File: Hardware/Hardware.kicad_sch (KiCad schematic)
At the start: 9 parts, among them J1 ILI9341, J2 RJ45_LED_Shielded, SW1 SW_SPST, U1 TMR-0511, U3 Teensy4.1_DEV-16771

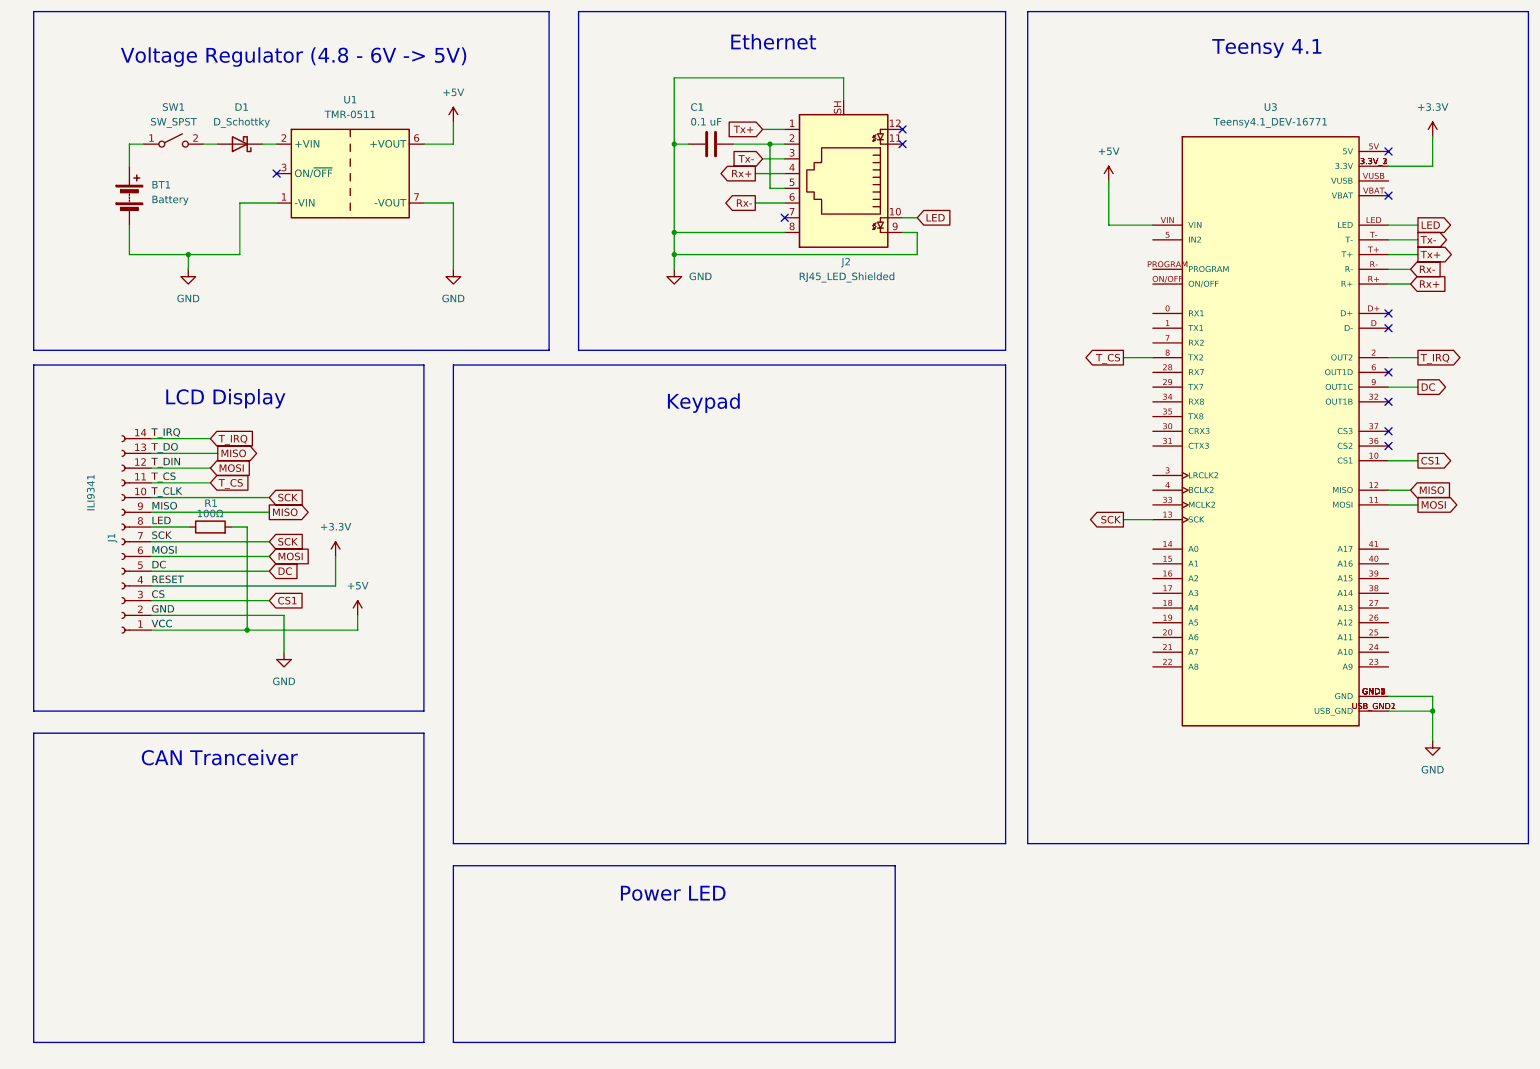
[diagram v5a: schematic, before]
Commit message: Added CAN tranceiver and keypad
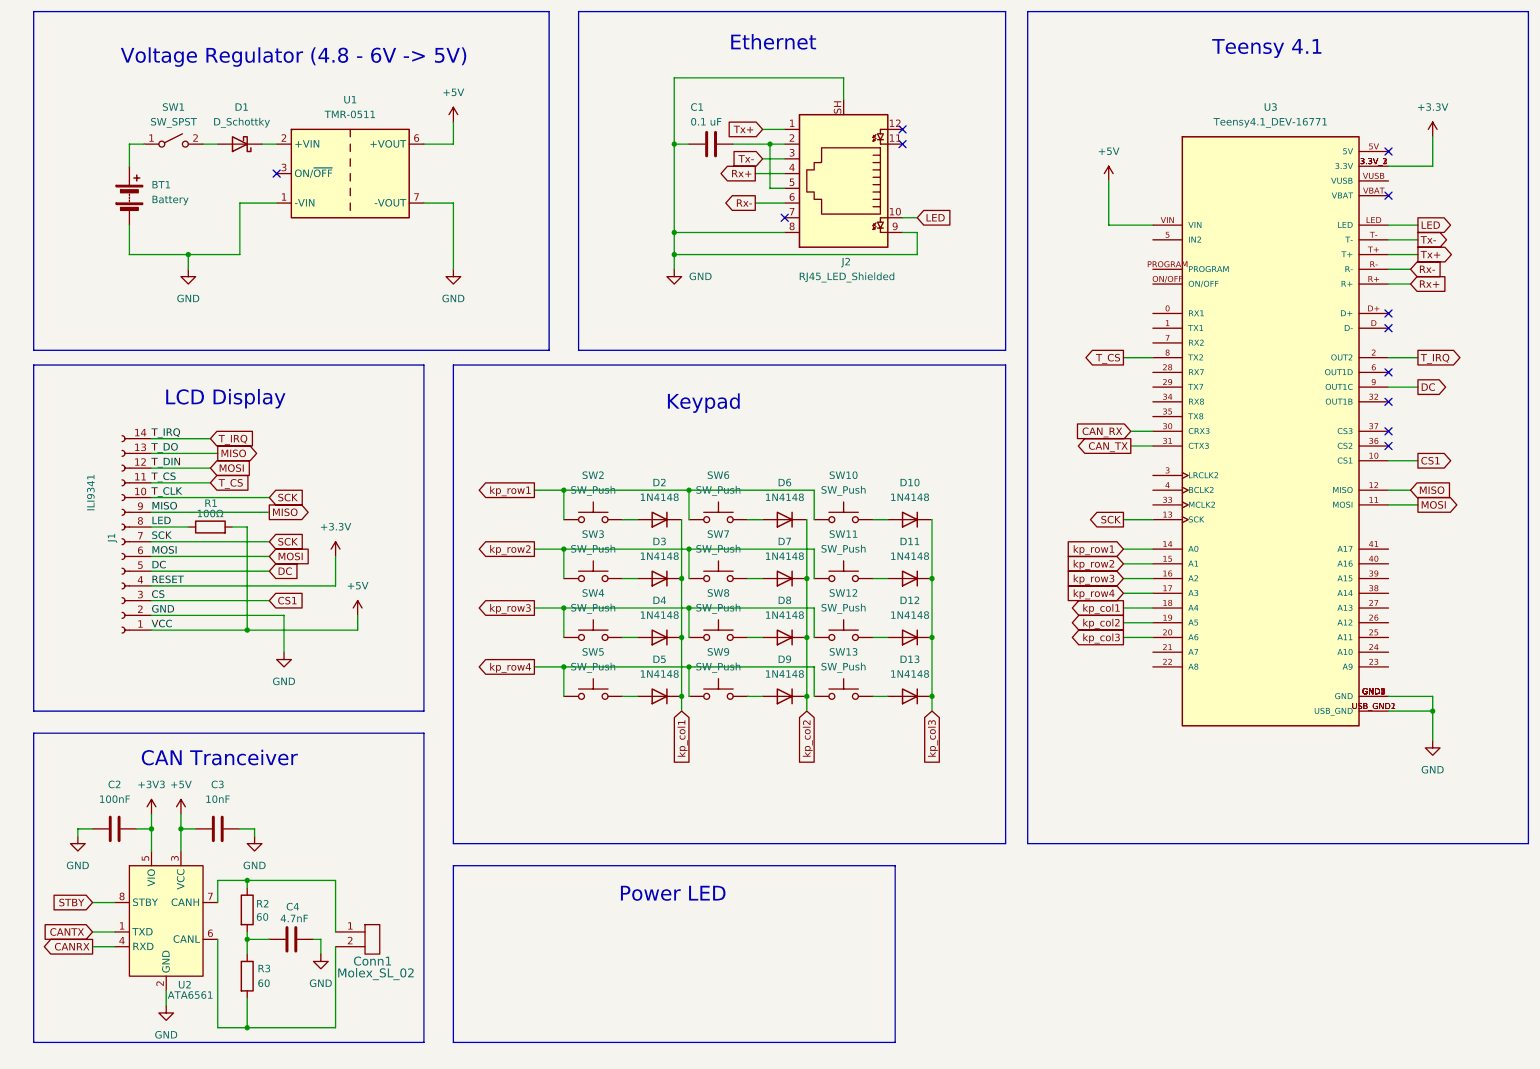
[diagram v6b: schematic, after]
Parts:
- added C2: 100nF, symbol Device:C
- added C3: 10nF, symbol Device:C
- added C4: 4.7nF, symbol Device:C
- added Conn1: Molex_SL_02, symbol MRDT_Connectors:Molex_SL_02
- added D10, D11, D12, D13, D2, D3, D4, D5, D6, D7, D8, D9: 1N4148, Diode_THT:D_DO-35_SOD27_P7.62mm_Horizontal, symbol Diode:1N4148
- added R2, R3: 60, symbol Device:R
- added SW10, SW11, SW12, SW13, SW2, SW3, SW4, SW5, SW6, SW7, SW8, SW9: SW_Push, symbol Switch:SW_Push
- added U2: ATA6561, Package_SO:SOIC-8_3.9x4.9mm_P1.27mm, symbol MRDT_Devices:ATA6561
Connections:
- net +5V: now also C3.1, U2.3 (VCC)
- net GND: now also C2.2, C3.2, C4.2, U2.2 (GND)
- net kp_row1: now reaches U3.14 (A0)
- net kp_row1: now also SW10.1, SW2.1, SW6.1
- net kp_row2: now reaches U3.15 (A1)
- net kp_row2: now also SW11.1, SW3.1, SW7.1
- net kp_row3: now reaches U3.16 (A2)
- net kp_row3: now also SW12.1, SW4.1, SW8.1
- net kp_row4: now reaches U3.17 (A3)
- net kp_row4: now also SW13.1, SW5.1, SW9.1
- net kp_col1: now reaches U3.18 (A4)
- net kp_col1: now also D2.1 (K), D3.1 (K), D4.1 (K), D5.1 (K)
- net kp_col2: now reaches U3.19 (A5)
- net kp_col2: now also D6.1 (K), D7.1 (K), D8.1 (K), D9.1 (K)
- net kp_col3: now reaches U3.20 (A6)
- net kp_col3: now also D10.1 (K), D11.1 (K), D12.1 (K), D13.1 (K)
- net CAN_RX: now reaches U3.30 (CRX3)
- net CAN_TX: now reaches U3.31 (CTX3)
- new net: D5.2 (A), SW5.2
- new net: Conn1.1, R2.1, U2.7 (CANH)
- new net: C4.1, R2.2, R3.1
- new net: D9.2 (A), SW9.2
- new net: D6.2 (A), SW6.2
- new net: D13.2 (A), SW13.2
- new net: D7.2 (A), SW7.2
- new net: D11.2 (A), SW11.2
- new net: D8.2 (A), SW8.2
- new net: Conn1.2, R3.2, U2.6 (CANL)
- new net: D4.2 (A), SW4.2
- new net: D3.2 (A), SW3.2
- new net: D2.2 (A), SW2.2
- new net: D10.2 (A), SW10.2
- new net: D12.2 (A), SW12.2
- new net +3V3: C2.1, U2.5 (VIO)
- new net CANRX: U2.4 (RXD)
- new net CANTX: U2.1 (TXD)
- new net STBY: U2.8 (STBY)

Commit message: Update Hardware.kicad_sch
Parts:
- added D14: LED, symbol Device:LED
- added R4: 220, symbol Device:R
- C3: value 10nF -> 100nF
- R1: value 100Ω -> 100
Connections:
- net +3V3 is gone; now on net +3.3V: C2.1, U2.5 (VIO)
- net GND is gone; now on net +5V: BT1.2 (-), C1.2, C2.2, C3.2, C4.2, J1.2 (Pin_2), J2.8, J2.9, J2.SH, U1.1 (-VIN), U1.7 (-VOUT), U2.2 (GND), U3.GND1 (GND), U3.GND2 (GND), U3.GND3 (GND), U3.GND4 (GND), U3.GND5 (GND), U3.USB_GND1 (USB_GND), U3.USB_GND2 (USB_GND)
- net +5V: now also U3.5V, D14.2 (A), R4.1
- net CAN_RX: now also U3.23 (A9); no longer U3.30 (CRX3)
- net CAN_TX: now also U3.22 (A8); no longer U3.31 (CTX3)
- new net: D14.1 (K), R4.2
- no-connect marks 12 -> 36

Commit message: Update Hardware.kicad_sch
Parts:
- R1, R2, R3, R4: footprint (none) -> Resistor_SMD:R_0603_1608Metric_Pad0.98x0.95mm_HandSolder
- U3: footprint MODULE_DEV-16771 -> MRDT_Shields:Teensy_4_1_Ethernet
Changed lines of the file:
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@@
 			)
 		)
-		(property "Footprint" ""
+		(property "Footprint" "Resistor_SMD:R_0603_1608Metric_Pad0.98x0.95mm_HandSolder"
 			(at 142.24 185.928 90)
 			(effects
@@
 			)
 		)
-		(property "Footprint" ""
+		(property "Footprint" "Resistor_SMD:R_0603_1608Metric_Pad0.98x0.95mm_HandSolder"
 			(at 57.912 170.18 90)
 			(effects
@@
 			)
 		)
-		(property "Footprint" ""
+		(property "Footprint" "Resistor_SMD:R_0603_1608Metric_Pad0.98x0.95mm_HandSolder"
 			(at 53.34 105.918 90)
 			(effects
@@
 			)
 		)
-		(property "Footprint" "MODULE_DEV-16771"
+		(property "Footprint" "MRDT_Shields:Teensy_4_1_Ethernet"
 			(at 289.56 95.25 0)
 			(effects
@@
 			)
 		)
-		(property "Footprint" ""
+		(property "Footprint" "Resistor_SMD:R_0603_1608Metric_Pad0.98x0.95mm_HandSolder"
 			(at 57.912 181.61 90)
 			(effects
